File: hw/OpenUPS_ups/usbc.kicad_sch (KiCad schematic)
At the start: 1 part, among them J1101 USB_C_Receptacle

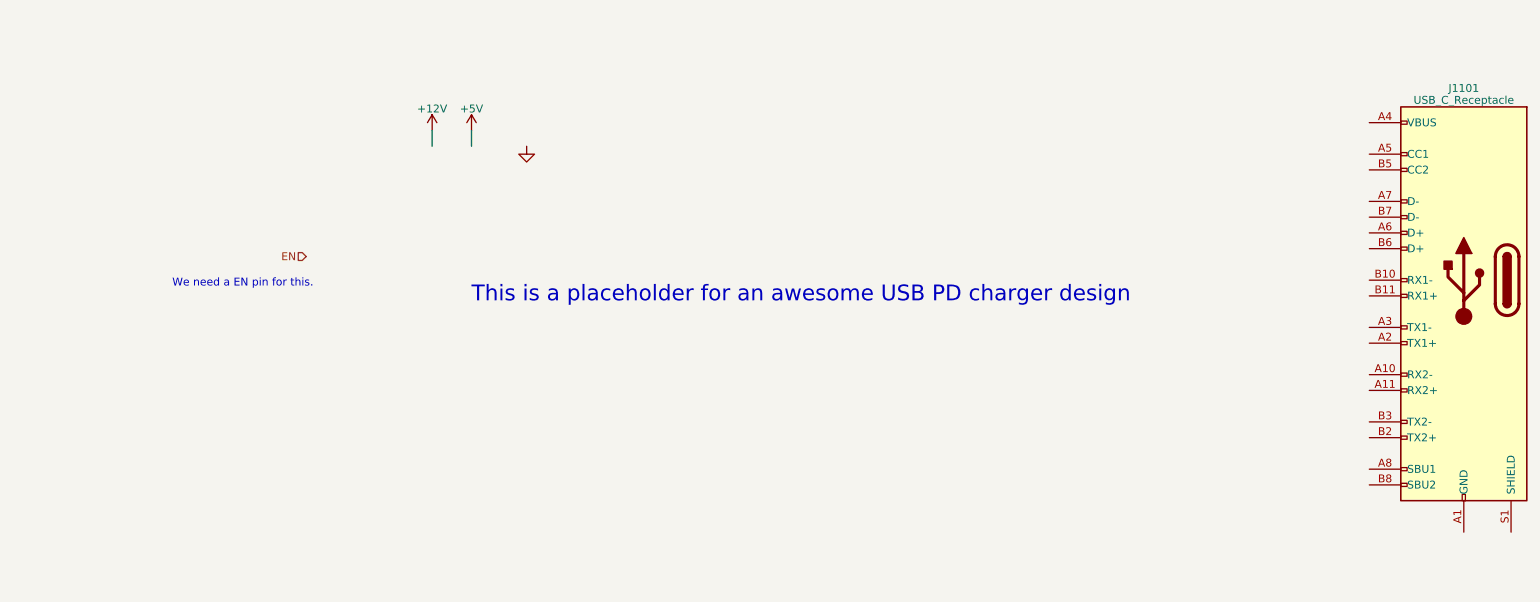
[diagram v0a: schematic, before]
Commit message: Issue #13, USB-C output, at last!
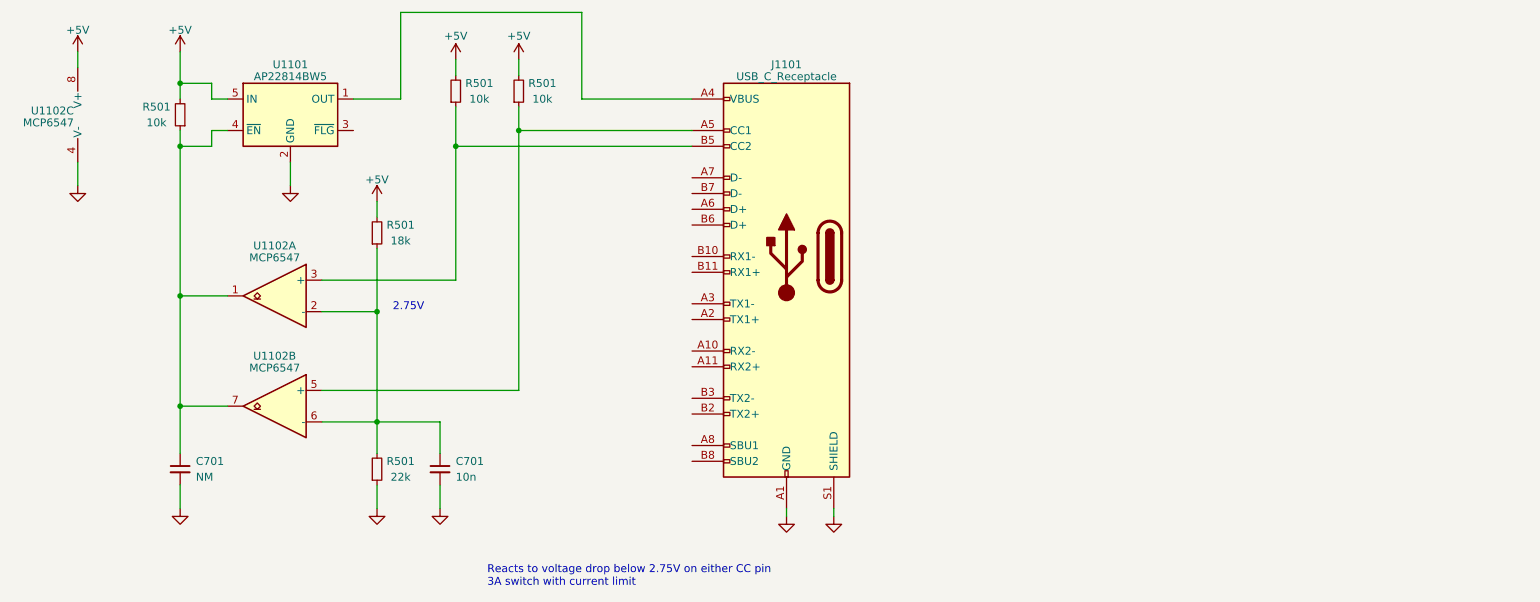
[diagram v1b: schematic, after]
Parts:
- added C701: 10n, Capacitor_SMD:C_0603_1608Metric, symbol Device:C_Small
- added C701: NM, Capacitor_SMD:C_0603_1608Metric, symbol Device:C_Small
- added R501: 18k, Resistor_SMD:R_0603_1608Metric, symbol Device:R_Small
- added R501 (x3): 10k, Resistor_SMD:R_0603_1608Metric, symbol Device:R_Small
- added R501: 22k, Resistor_SMD:R_0603_1608Metric, symbol Device:R_Small
- added U1101: AP22814BW5, Package_TO_SOT_SMD:SOT-23-5, symbol Power_Management:AP22814BW5
- added U1102: MCP6547, Package_SO:SO-8_3.9x4.9mm_P1.27mm, symbol Comparator:MCP6567
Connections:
- net +5V: now also R501.2, R501.2, R501.2, R501.2, U1101.5 (IN), U1102.8 (V+)
- net GND: now also J1101.A1 (GND), J1101.A12 (GND), J1101.B1 (GND), J1101.B12 (GND), J1101.S1 (SHIELD), C701.2, C701.2, R501.1, U1101.2 (GND), U1102.4 (V-)
- net at J1101.A4 (VBUS), J1101.A9 (VBUS), J1101.B4 (VBUS)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: now also U1101.1 (OUT)
- net at J1101.A5 (CC1): now also R501.1, U1102.5 (+)
- net at J1101.B5 (CC2): now also R501.1, U1102.3 (+)
- new net: C701.1, R501.1, R501.2, U1102.2 (-), U1102.6 (-)
- new net: C701.1, R501.1, U1101.4 (~{EN}), U1102.1, U1102.7
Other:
- note added: "2.75V"
- note added: "Reacts to voltage drop below 2.75V on either CC pin 3A switch with current limit"
- note removed: "This is a placeholder for an awesome USB PD charger design"
- note removed: "We need a EN pin for this."
- moved on the sheet: J1101

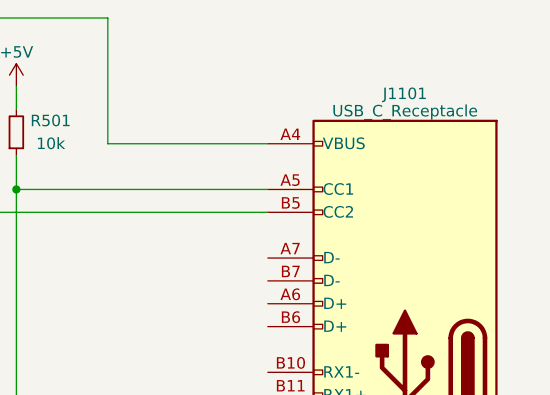
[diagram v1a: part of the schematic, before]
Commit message: Preliminary NMOS: AON7534; USB-C selected.
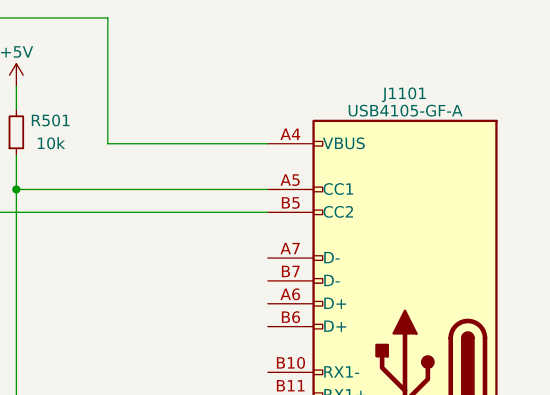
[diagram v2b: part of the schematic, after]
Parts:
- J1101: value USB_C_Receptacle -> USB4105-GF-A; footprint (none) -> Connector_USB:USB_C_Receptacle_GCT_USB4105-xx-A_16P_TopMnt_Horizontal
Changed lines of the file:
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@@
       (effects (font (size 1.27 1.27)))
     )
-    (property "Value" "USB_C_Receptacle" (at 139.7 26.8511 0)
+    (property "Value" "USB4105-GF-A" (at 139.7 26.8511 0)
       (effects (font (size 1.27 1.27)))
     )
-    (property "Footprint" "" (at 135.89 55.88 0)
+    (property "Footprint" "Connector_USB:USB_C_Receptacle_GCT_USB4105-xx-A_16P_TopMnt_Horizontal" (at 135.89 55.88 0)
       (effects (font (size 1.27 1.27)) hide)
     )
-    (property "Datasheet" "https://www.usb.org/sites/default/files/documents/usb_type-c.zip" (at 135.89 55.88 0)
+    (property "Datasheet" "" (at 135.89 55.88 0)
       (effects (font (size 1.27 1.27)) hide)
     )

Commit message: Initial placement effort
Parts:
- renumbered J1101 to J1001, U1102 to U1001, U1101 to U1002
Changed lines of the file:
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@@
         )
         (path "/f77faec3-eac4-47f3-a2de-ec4a039f4502/5d533980-99bb-4871-b1d2-8a68cd48eb84"
-          (reference "R1104") (unit 1)
+          (reference "R1002") (unit 1)
         )
       )
@@
         )
         (path "/f77faec3-eac4-47f3-a2de-ec4a039f4502/5d533980-99bb-4871-b1d2-8a68cd48eb84"
-          (reference "#PWR01105") (unit 1)
+          (reference "#PWR01009") (unit 1)
         )
       )
@@
         )
         (path "/f77faec3-eac4-47f3-a2de-ec4a039f4502/5d533980-99bb-4871-b1d2-8a68cd48eb84"
-          (reference "#PWR01104") (unit 1)
+          (reference "#PWR01012") (unit 1)
         )
       )
@@
   (symbol (lib_id "Comparator:MCP6567") (at 22.86 33.02 0) (mirror y) (unit 3)
     (in_bom yes) (on_board yes) (dnp no)
-    (property "Reference" "U1102" (at 24.765 32.3763 0)
+    (property "Reference" "U1001" (at 24.765 32.3763 0)
       (effects (font (size 1.27 1.27)) (justify left))
     )
@@
       (project "OpenUPS_ups"
         (path "/f77faec3-eac4-47f3-a2de-ec4a039f4502/5d533980-99bb-4871-b1d2-8a68cd48eb84"
-          (reference "U1102") (unit 3)
+          (reference "U1001") (unit 3)
         )
       )
@@
         )
         (path "/f77faec3-eac4-47f3-a2de-ec4a039f4502/5d533980-99bb-4871-b1d2-8a68cd48eb84"
-          (reference "R1101") (unit 1)
+          (reference "R1005") (unit 1)
         )
       )
@@
   (symbol (lib_id "Comparator:MCP6567") (at 57.15 62.23 0) (mirror y) (unit 1)
     (in_bom yes) (on_board yes) (dnp no)
-    (property "Reference" "U1102" (at 57.15 54.1401 0)
+    (property "Reference" "U1001" (at 57.15 54.1401 0)
       (effects (font (size 1.27 1.27)))
     )
@@
       (project "OpenUPS_ups"
         (path "/f77faec3-eac4-47f3-a2de-ec4a039f4502/5d533980-99bb-4871-b1d2-8a68cd48eb84"
-          (reference "U1102") (unit 1)
+          (reference "U1001") (unit 1)
         )
       )
@@
         )
         (path "/f77faec3-eac4-47f3-a2de-ec4a039f4502/5d533980-99bb-4871-b1d2-8a68cd48eb84"
-          (reference "#PWR01112") (unit 1)
+          (reference "#PWR01004") (unit 1)
         )
       )
@@
   (symbol (lib_id "Comparator:MCP6567") (at 57.15 80.01 0) (mirror y) (unit 2)
     (in_bom yes) (on_board yes) (dnp no)
-    (property "Reference" "U1102" (at 57.15 71.9201 0)
+    (property "Reference" "U1001" (at 57.15 71.9201 0)
       (effects (font (size 1.27 1.27)))
     )
@@
       (project "OpenUPS_ups"
         (path "/f77faec3-eac4-47f3-a2de-ec4a039f4502/5d533980-99bb-4871-b1d2-8a68cd48eb84"
-          (reference "U1102") (unit 2)
+          (reference "U1001") (unit 2)
         )
       )
@@
         )
         (path "/f77faec3-eac4-47f3-a2de-ec4a039f4502/5d533980-99bb-4871-b1d2-8a68cd48eb84"
-          (reference "C1101") (unit 1)
+          (reference "C1002") (unit 1)
         )
       )
@@
         )
         (path "/f77faec3-eac4-47f3-a2de-ec4a039f4502/5d533980-99bb-4871-b1d2-8a68cd48eb84"
-          (reference "R1103") (unit 1)
+          (reference "R1001") (unit 1)
         )
       )
@@
         )
         (path "/f77faec3-eac4-47f3-a2de-ec4a039f4502/5d533980-99bb-4871-b1d2-8a68cd48eb84"
-          (reference "#PWR01106") (unit 1)
+          (reference "#PWR01010") (unit 1)
         )
       )
@@
         )
         (path "/f77faec3-eac4-47f3-a2de-ec4a039f4502/5d533980-99bb-4871-b1d2-8a68cd48eb84"
-          (reference "R1105") (unit 1)
+          (reference "R1003") (unit 1)
         )
       )
@@
         )
         (path "/f77faec3-eac4-47f3-a2de-ec4a039f4502/5d533980-99bb-4871-b1d2-8a68cd48eb84"
-          (reference "#PWR01110") (unit 1)
+          (reference "#PWR01006") (unit 1)
         )
       )
@@
         )
         (path "/f77faec3-eac4-47f3-a2de-ec4a039f4502/5d533980-99bb-4871-b1d2-8a68cd48eb84"
-          (reference "#PWR01109") (unit 1)
+          (reference "#PWR01007") (unit 1)
         )
       )
@@
         )
         (path "/f77faec3-eac4-47f3-a2de-ec4a039f4502/5d533980-99bb-4871-b1d2-8a68cd48eb84"
-          (reference "#PWR01108") (unit 1)
+          (reference "#PWR01002") (unit 1)
         )
       )
@@
         )
         (path "/f77faec3-eac4-47f3-a2de-ec4a039f4502/5d533980-99bb-4871-b1d2-8a68cd48eb84"
-          (reference "#PWR01107") (unit 1)
+          (reference "#PWR01001") (unit 1)
         )
       )
@@
         )
         (path "/f77faec3-eac4-47f3-a2de-ec4a039f4502/5d533980-99bb-4871-b1d2-8a68cd48eb84"
-          (reference "#PWR01111") (unit 1)
+          (reference "#PWR01008") (unit 1)
         )
       )
@@
   (symbol (lib_id "Power_Management:AP22814BW5") (at 59.69 33.02 0) (unit 1)
     (in_bom yes) (on_board yes) (dnp no) (fields_autoplaced)
-    (property "Reference" "U1101" (at 59.69 24.9301 0)
+    (property "Reference" "U1002" (at 59.69 24.9301 0)
       (effects (font (size 1.27 1.27)))
     )
@@
       (project "OpenUPS_ups"
         (path "/f77faec3-eac4-47f3-a2de-ec4a039f4502/5d533980-99bb-4871-b1d2-8a68cd48eb84"
-          (reference "U1101") (unit 1)
+          (reference "U1002") (unit 1)
         )
       )
@@
   (symbol (lib_id "Connector:USB_C_Receptacle") (at 139.7 55.88 0) (mirror y) (unit 1)
     (in_bom yes) (on_board yes) (dnp no)
-    (property "Reference" "J1101" (at 139.7 24.9301 0)
+    (property "Reference" "J1001" (at 139.7 24.9301 0)
       (effects (font (size 1.27 1.27)))
     )
@@
       (project "OpenUPS_ups"
         (path "/f77faec3-eac4-47f3-a2de-ec4a039f4502/5d533980-99bb-4871-b1d2-8a68cd48eb84"
-          (reference "J1101") (unit 1)
+          (reference "J1001") (unit 1)
         )
       )
@@
         )
         (path "/f77faec3-eac4-47f3-a2de-ec4a039f4502/5d533980-99bb-4871-b1d2-8a68cd48eb84"
-          (reference "R1102") (unit 1)
+          (reference "R1004") (unit 1)
         )
       )
@@
         )
         (path "/f77faec3-eac4-47f3-a2de-ec4a039f4502/5d533980-99bb-4871-b1d2-8a68cd48eb84"
-          (reference "#PWR01102") (unit 1)
+          (reference "#PWR01003") (unit 1)
         )
       )
@@
         )
         (path "/f77faec3-eac4-47f3-a2de-ec4a039f4502/5d533980-99bb-4871-b1d2-8a68cd48eb84"
-          (reference "#PWR01103") (unit 1)
+          (reference "#PWR01005") (unit 1)
         )
       )
@@
         )
         (path "/f77faec3-eac4-47f3-a2de-ec4a039f4502/5d533980-99bb-4871-b1d2-8a68cd48eb84"
-          (reference "#PWR01101") (unit 1)
+          (reference "#PWR01011") (unit 1)
         )
       )
@@
         )
         (path "/f77faec3-eac4-47f3-a2de-ec4a039f4502/5d533980-99bb-4871-b1d2-8a68cd48eb84"
-          (reference "C1102") (unit 1)
-        )
-      )
+          (reference "C1001") (unit 1)
+        )
+      )

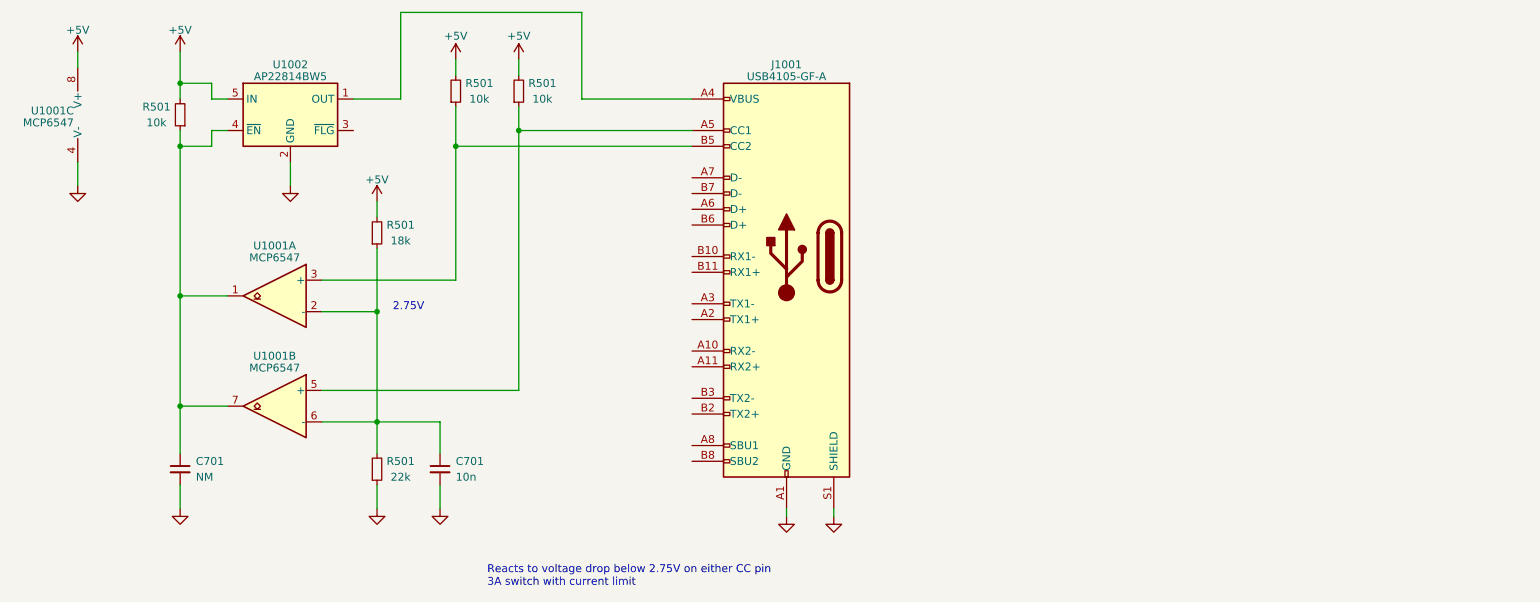
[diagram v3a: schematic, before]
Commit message: Issue #30: USB Force ON feature
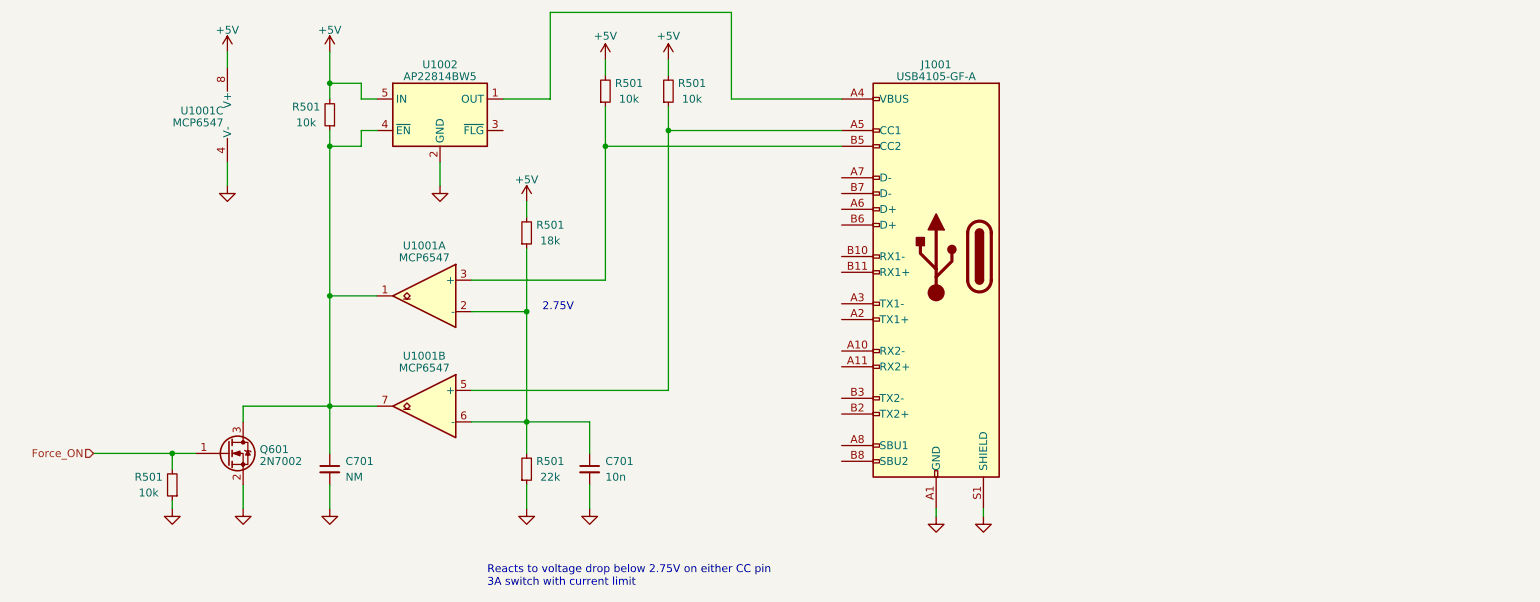
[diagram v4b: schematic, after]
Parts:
- added Q601: 2N7002, Package_TO_SOT_SMD:SOT-23, symbol Transistor_FET:2N7002
- added R501: 10k, Resistor_SMD:R_0603_1608Metric, symbol Device:R_Small
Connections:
- net GND: now also Q601.2 (S), R501.1
- net at C701.1, R501.1, U1001.1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: now also Q601.3 (D)
- new net Force_ON: Q601.1 (G), R501.2
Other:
- moved on the sheet: C701, J1001, R501, U1001A, U1001B, U1001C, U1002
